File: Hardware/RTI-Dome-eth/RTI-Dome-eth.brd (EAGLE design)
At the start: 119.4 x 71.2 mm, 85 parts, among them IC1 24AA128ST, IC3 FT232RL, IC4 REG1117-3.3/2K5, IC5 74LVC245, IC6 74ABT245, J1 POWERPOLE_POWER45A, U1 W5500, X13 PN61729-S, X9 J1011F21PNL

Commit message: Fix merge conflict
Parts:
- 25MHZ: value CB3LV-3I-25M0000 -> CB3LV-OSCILATOR
- IC4: value REG1117-3.3/2K5 -> REG1117
- R1, R3: value 2.2K -> 1K
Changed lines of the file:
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@@
 <attribute name="OC_FARNELL" value="unknown" x="-2.9845" y="55.91175" size="1.778" layer="27" display="off"/>
 </element>
-<element name="R1" library="rti" package="R0805" value="2.2K" x="7.58825" y="44.45" rot="R270">
+<element name="R1" library="rti" package="R0805" value="1K" x="7.58825" y="44.45" rot="R270">
 <attribute name="MPN" value="RT0805FRE071KL" x="7.58825" y="44.45" size="1.778" layer="27" rot="R270" display="off"/>
 </element>
-<element name="R3" library="rti" package="R0805" value="2.2K" x="1.93675" y="44.45" rot="R270">
+<element name="R3" library="rti" package="R0805" value="1K" x="1.93675" y="44.45" rot="R270">
 <attribute name="MPN" value="RT0805FRE071KL" x="1.93675" y="44.45" size="1.778" layer="27" rot="R270" display="off"/>
 </element>
@@
 </element>
 <element name="J1" library="powerpoles" package="POWERPOLE_PAIR_45A" value="POWERPOLE_POWER45A" x="102.87" y="8.89" rot="MR90"/>
-<element name="25MHZ" library="rti" package="SMD-7050_4P" value="CB3LV-3I-25M0000" x="58.42" y="27.94">
+<element name="25MHZ" library="rti" package="SMD-7050_4P" value="CB3LV-OSCILATOR" x="58.42" y="27.94">
 <attribute name="MPN" value="CB3LV-3I-25M0000" x="58.42" y="27.94" size="1.778" layer="27" display="off"/>
 </element>
@@
 <attribute name="MPN" value="BLM21AG121SN1D" x="78.74" y="13.97" size="1.778" layer="27" rot="R180" display="off"/>
 </element>
-<element name="IC4" library="burr-brown" package="SOT223" value="REG1117-3.3/2K5" x="50.8" y="21.59" rot="R180">
+<element name="IC4" library="burr-brown" package="SOT223" value="REG1117" x="50.8" y="21.59" rot="R180">
 <attribute name="MPN" value="REG1117-3.3/2K5" x="50.8" y="21.59" size="1.778" layer="27" rot="R180" display="off"/>
 <attribute name="MF" value="" x="50.8" y="21.59" size="1.778" layer="27" rot="R180" display="off"/>

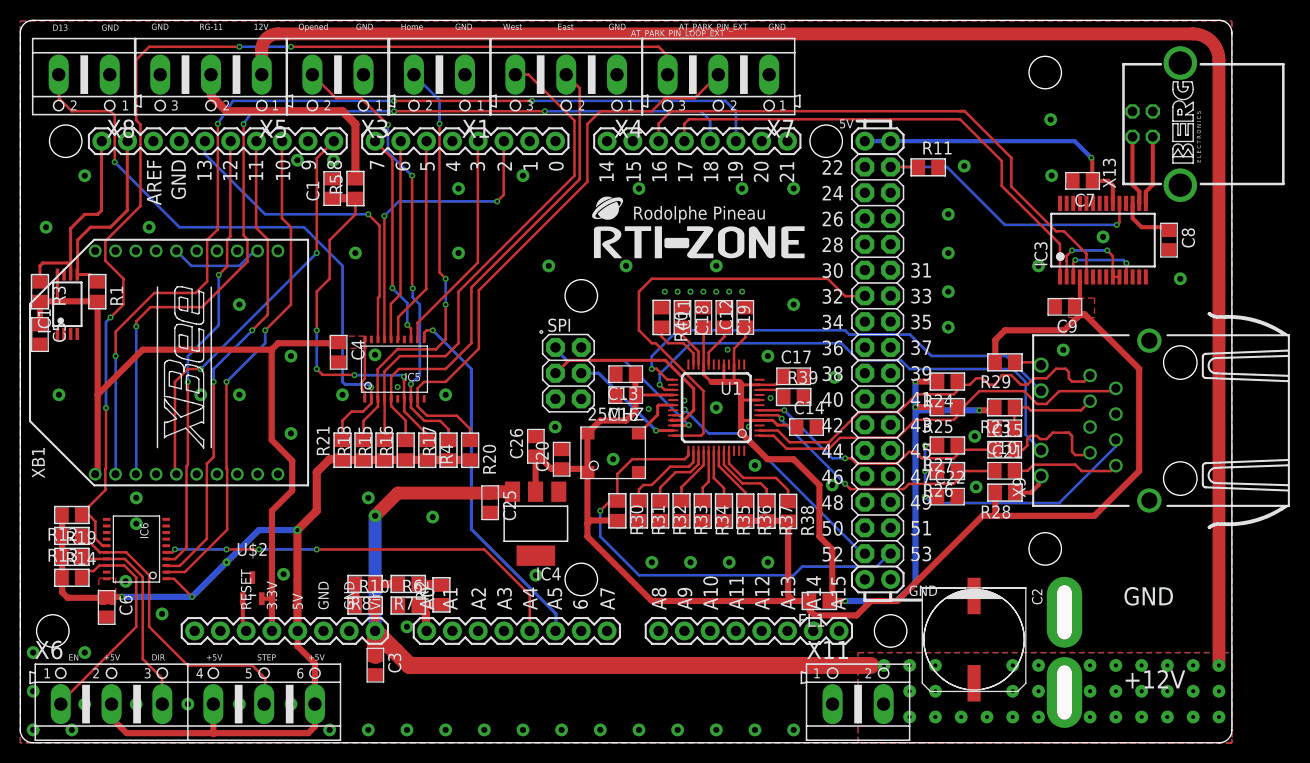
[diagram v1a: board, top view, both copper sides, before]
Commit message: Fix a  bug when reading number of step per rev after new firnware changes.
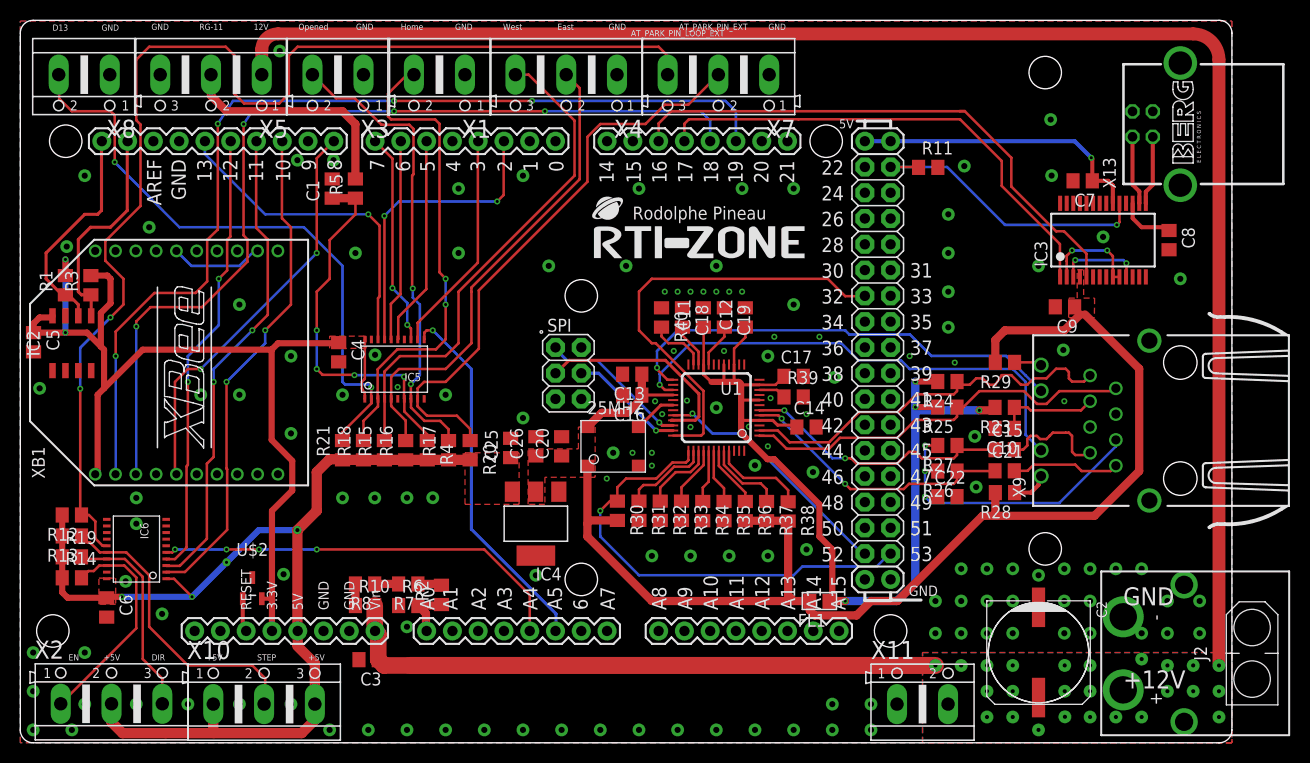
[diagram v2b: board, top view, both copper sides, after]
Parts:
- removed IC1: 24AA128ST, microchip:TSSOP8
- removed J1: POWERPOLE_POWER45A, powerpoles:POWERPOLE_PAIR_45A
- removed X6: (no value), con-ptr500:AK500/6
- added IC2: 24LC128T-I_SN, rti:SOIC127P600X175-8N
- added J2: XT60PW-M, samacsys:XT60PWM
- added X10, X2: (no value), rti:AK500/3
- C1, C10, C11, C12, C13, C14, C15, C16, C17, C18, C19, C20, C21, C22, C25, C26, C3, C4, C5, C6, C7, C8, C9: device rti:C0805 -> rcl:C0805
- C2: device rti:UD-10X10_NICHICON -> samacsys:UD-10X10_NICHICON
- R1, R10, R11, R12, R13, R14, R15, R16, R17, R18, R19, R2, R20, R21, R23, R24, R25, R26, R27, R28, R29, R3, R30, R31, R32, R33, R34, R35, R36, R37, R38, R39, R4, R40, R5, R6, R7, R8: device rti:R0805 -> rcl:R0805
- U$2: value MCP120T-270I_TT -> MCP120T; device MCP120T-270I_TT:SOT95P237X112-3N -> MCP120T:SOT95P237X112-3N
- X1, X11, X3, X8: device con-ptr500:AK500/2 -> rti:AK500/2
- X13: device con-berg:PN61729-S -> rti:PN61729-S
- X4, X5, X7: device con-ptr500:AK500/3 -> rti:AK500/3
- XB1: device maxstream:XBEE -> rti:XBEE
- moved C2 6.48 mm to (100.3, 8.89)
- moved X11 6.35 mm to (88.9, 3.81)
- moved C25 5.76 mm to (48.3, 29.1), turned to 90 degrees
- moved R3 5.06 mm to (6.95, 45.1), turned to 90 degrees
- moved R1 3.21 mm to (4.45, 45.1), turned to 90 degrees
- moved C20 1.27 mm to (53.3, 29.2)
- moved C5 0.99 mm to (1.30, 39.5)
- moved C3 0.86 mm to (34.3, 8.19), turned to 180 degrees
- moved 25MHZ 0.63 mm to (58.4, 28.6)
- moved C13 0.63 mm to (60.3, 36.3)
- moved C16 0.63 mm to (60.3, 34.3)
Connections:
- net +12V: now also J2.2; no longer C25.1, IC4.3, J1.RED
- net 3.3V: now also IC2.8; no longer IC1.8
- net GND: now also IC2.1, IC2.2, IC2.3, IC2.4, J2.1; no longer IC1.1, IC1.2, IC1.3, IC1.4, J1.BLACK
- net M_DIR_5V: now also X2.3; no longer X6.3
- net M_EN_5V: now also X2.1; no longer X6.1
- net M_STEP_5V: now also X10.2; no longer X6.5
- net SCL: now also IC2.6, R1.1; no longer IC1.6, R3.1
- net SDA: now also IC2.5, R3.1; no longer IC1.5, R1.1
- net VCC: now also C25.1, IC4.3, X10.1, X10.3, X2.2; no longer X6.2, X6.4, X6.6
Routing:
- net +12V: track 239.2 -> 218.8 mm, vias 34 -> 25
- net +3V3: track 146.7 -> 130.4 mm
- net 3.3V: track 90.3 -> 102.9 mm, vias 0 -> 2
- net AT_PARK_PIN_LOOP_EXT: track 108.6 -> 117.9 mm, vias 4 -> 2
- net HOME_SHUTTER_CLOSED_5V: track 42.9 -> 48.0 mm, vias 3 -> 2
- net SDI: track 18.6 -> 14.9 mm
- net SDA: track 18.6 -> 21.4 mm
- net SCL: track 20.0 -> 22.4 mm
- net SHUTTER_OPENED_5V: track 44.7 -> 46.1 mm, vias 4 -> 2
- net AVDD: track 96.8 -> 95.7 mm
- net SCLK: track 20.2 -> 21.3 mm
- net D13_EXT: track 61.5 -> 60.7 mm
- net ETH_CS: track 25.5 -> 24.7 mm
- net XI: track 5.01 -> 4.26 mm
- net AT_PARK_PIN_EXT: track 58.2 -> 57.4 mm
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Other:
- board text added: "Dome Rotator / RoR"
- board text removed: "Dome Rotator"

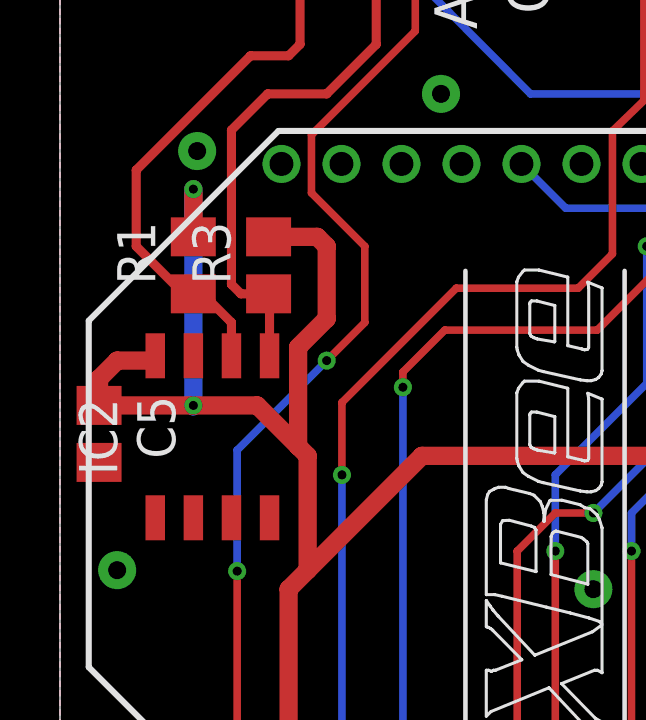
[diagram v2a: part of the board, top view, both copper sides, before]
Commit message: Set the shuuter response to open when there is no shutter controler
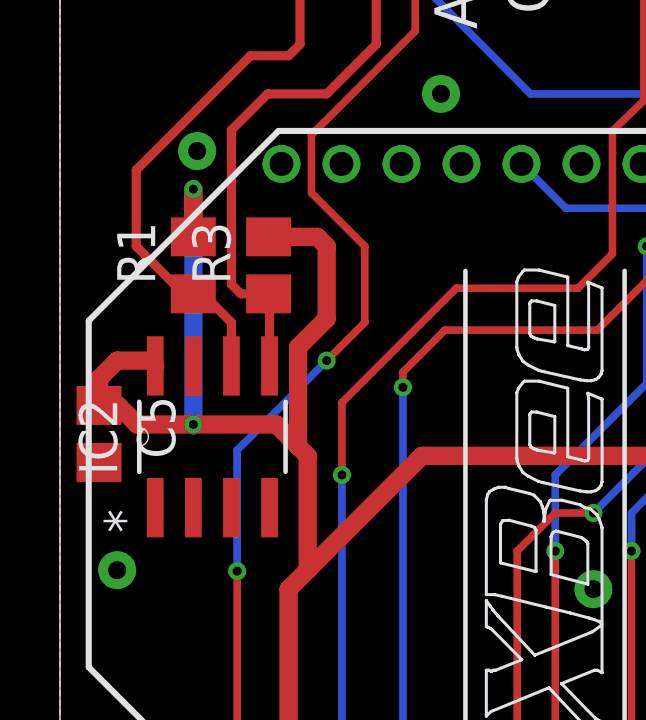
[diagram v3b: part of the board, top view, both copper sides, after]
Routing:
- net 3.3V: track 102.9 -> 103.5 mm
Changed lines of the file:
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@@
 <layer number="128" name="_bValues" color="7" fill="1" visible="yes" active="yes"/>
 <layer number="129" name="Mask" color="7" fill="1" visible="yes" active="yes"/>
+<layer number="130" name="SMDSTROOK" color="7" fill="1" visible="yes" active="yes"/>
 <layer number="131" name="tAdjust" color="7" fill="1" visible="yes" active="yes"/>
 <layer number="132" name="bAdjust" color="7" fill="1" visible="yes" active="yes"/>
+<layer number="133" name="bottom_silk" color="7" fill="1" visible="yes" active="yes"/>
+<layer number="134" name="silk_top" color="7" fill="1" visible="yes" active="yes"/>
+<layer number="135" name="silk_bottom" color="7" fill="1" visible="yes" active="yes"/>
+<layer number="136" name="silktop" color="7" fill="1" visible="yes" active="yes"/>
+<layer number="137" name="silkbottom" color="7" fill="1" visible="yes" active="yes"/>
 <layer number="144" name="Drill_legend" color="7" fill="1" visible="yes" active="yes"/>
+<layer number="145" name="DrillLegend_01-16" color="7" fill="1" visible="yes" active="yes"/>
+<layer number="146" name="DrillLegend_01-20" color="7" fill="1" visible="yes" active="yes"/>
 <layer number="150" name="Notes" color="7" fill="1" visible="yes" active="yes"/>
 <layer number="151" name="HeatSink" color="7" fill="1" visible="yes" active="yes"/>
@@
 <attribute name="VALUE" x="9.91" y="21.705" size="0.8128" layer="27" font="vector" rot="R270"/>
 </element>
-<element name="U$1" library="arduino_shield" library_urn="urn:adsk.eagle:library:37505075" package="ARDUINO_DUE_SHIELD_FULL" package3d_urn="urn:adsk.eagle:package:37505088/2" value="ARDUINO_DUE_SHIELD_FULL" x="38.76675" y="35.14725" smashed="yes"/>
+<element name="U$1" library="arduino_shield" library_urn="urn:adsk.eagle:library:37505075" package="ARDUINO_DUE_SHIELD_FULL" package3d_urn="urn:adsk.eagle:package:37505088/4" value="ARDUINO_DUE_SHIELD_FULL" x="38.76675" y="35.14725" smashed="yes"/>
 <element name="U1" library="W5500" library_urn="urn:adsk.eagle:library:37501005" package="LQFP48" package3d_urn="urn:adsk.eagle:package:37501008/2" value="W5500" x="68.58" y="33.02" smashed="yes" rot="R180">
 <attribute name="MPN" value="W5500" x="68.58" y="33.02" size="1.778" layer="27" rot="R180" display="off"/>
@@
 <attribute name="VALUE" x="16.4254" y="-1.9035" size="1.778" layer="27" ratio="10"/>
 </element>
-<element name="IC2" library="rti" library_urn="urn:adsk.eagle:library:37256580" package="SOIC127P600X175-8N" package3d_urn="urn:adsk.eagle:package:37894665/2" value="24LC128T-I_SN" x="5.08" y="39.37" smashed="yes" rot="R90">
+<element name="IC2" library="rti" library_urn="urn:adsk.eagle:library:37256580" package="SOIC127P600X175-8N" package3d_urn="urn:adsk.eagle:package:37894665/3" value="24LC128T-I_SN" x="5.08" y="39.37" smashed="yes" rot="R90">
 <attribute name="ARROW_PART_NUMBER" value="24LC128T-I/SN" x="5.08" y="39.37" size="1.778" layer="27" rot="R90" display="off"/>
 <attribute name="ARROW_PRICE-STOCK" value="https://www.arrow.com/en/products/24lc128t-isn/microchip-technology?region=nac" x="5.08" y="39.37" size="1.778" layer="27" rot="R90" display="off"/>
@@
 <wire x1="31.308" y1="39.37" x2="25.4" y2="39.37" width="0.6096" layer="1"/>
 <contactref element="IC2" pad="8"/>
-<wire x1="3.175" y1="42.07" x2="3.015" y2="41.91" width="0.6096" layer="1"/>
+<wire x1="3.175" y1="41.7322" x2="3.015" y2="41.91" width="0.6096" layer="1"/>
 <wire x1="3.015" y1="41.91" x2="1.905" y2="41.91" width="0.6096" layer="1"/>
 <wire x1="1.905" y1="41.91" x2="1.30175" y2="41.30675" width="0.6096" layer="1"/>
 <wire x1="1.30175" y1="41.30675" x2="1.30175" y2="40.41525" width="0.6096" layer="1"/>
-<wire x1="1.30175" y1="40.41525" x2="4.445" y2="40.41525" width="0.6096" layer="1"/>
-<wire x1="4.445" y1="40.41525" x2="6.57475" y2="40.41525" width="0.6096" layer="1"/>
-<wire x1="6.57475" y1="40.41525" x2="7.9375" y2="39.0525" width="0.6096" layer="1"/>
+<wire x1="1.30175" y1="40.41525" x2="1.93675" y2="40.41525" width="0.6096" layer="1"/>
+<wire x1="2.57175" y1="39.78025" x2="1.93675" y2="40.41525" width="0.6096" layer="1"/>
+<wire x1="4.445" y1="39.78025" x2="2.57175" y2="39.78025" width="0.6096" layer="1"/>
+<wire x1="7.20975" y1="39.78025" x2="4.445" y2="39.78025" width="0.6096" layer="1"/>
+<wire x1="7.20975" y1="39.78025" x2="7.9375" y2="39.0525" width="0.6096" layer="1"/>
 <wire x1="7.9375" y1="39.0525" x2="8.255" y2="38.735" width="0.6096" layer="1"/>
 <wire x1="8.255" y1="38.735" x2="8.255" y2="34.925" width="0.6096" layer="1"/>
@@
 <wire x1="4.445" y1="46.035" x2="4.445" y2="47.625" width="0.6096" layer="1"/>
 <via x="4.445" y="47.625" extent="1-16" drill="0.3"/>
-<wire x1="4.445" y1="47.625" x2="4.445" y2="40.41525" width="0.6096" layer="16"/>
-<wire x1="4.445" y1="40.386" x2="4.445" y2="40.41525" width="0.6096" layer="16"/>
-<wire x1="4.445" y1="40.41525" x2="4.445" y2="40.386" width="0.6096" layer="16"/>
-<via x="4.445" y="40.41525" extent="1-16" drill="0.3"/>
+<wire x1="4.445" y1="47.625" x2="4.445" y2="39.78025" width="0.6096" layer="16"/>
+<wire x1="4.445" y1="39.751" x2="4.445" y2="39.78025" width="0.6096" layer="16"/>
+<wire x1="4.445" y1="39.751" x2="4.445" y2="39.78025" width="0.6096" layer="16"/>
+<via x="4.445" y="39.78025" extent="1-16" drill="0.3"/>
 </signal>
 <signal name="RG-11-IN_5V">
@@
 <wire x1="6.03" y1="44.135" x2="6.95325" y2="44.135" width="0.3048" layer="1"/>
 <wire x1="6.95325" y1="44.135" x2="6.985" y2="44.10325" width="0.3048" layer="1"/>
-<wire x1="6.985" y1="44.10325" x2="6.985" y2="42.07" width="0.3048" layer="1"/>
+<wire x1="6.985" y1="44.10325" x2="6.985" y2="41.7322" width="0.3048" layer="1"/>
 </signal>
 <signal name="SCL">
@@
 <wire x1="3.998" y1="44.262" x2="4.125" y2="44.135" width="0.3048" layer="1"/>
 <wire x1="4.125" y1="44.135" x2="4.445" y2="44.135" width="0.3048" layer="1"/>
-<wire x1="5.715" y1="42.07" x2="5.715" y2="43.18" width="0.3048" layer="1"/>
+<wire x1="5.715" y1="41.7322" x2="5.715" y2="43.18" width="0.3048" layer="1"/>
 <wire x1="5.715" y1="43.18" x2="4.633" y2="44.262" width="0.3048" layer="1"/>
 <wire x1="4.633" y1="44.262" x2="3.998" y2="44.262" width="0.3048" layer="1"/>
